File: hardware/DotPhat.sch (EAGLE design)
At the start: 61 parts, among them CN1 1X4-BIG, IC1 CAT24M010TS, IC3 SI1145, J2 RASPBERRYPI-40-PIN-GPIO_PTH, J3 USB-MICROB, Q1 BSH103, U1 ATMEGA328P-MU-QFN32, U2 TMP102, U3 ATSHA204-TSU, U4 W25Q32FV, X2 MC-RTC-RV-4162-C7-I2C, X3 S4B-ZR

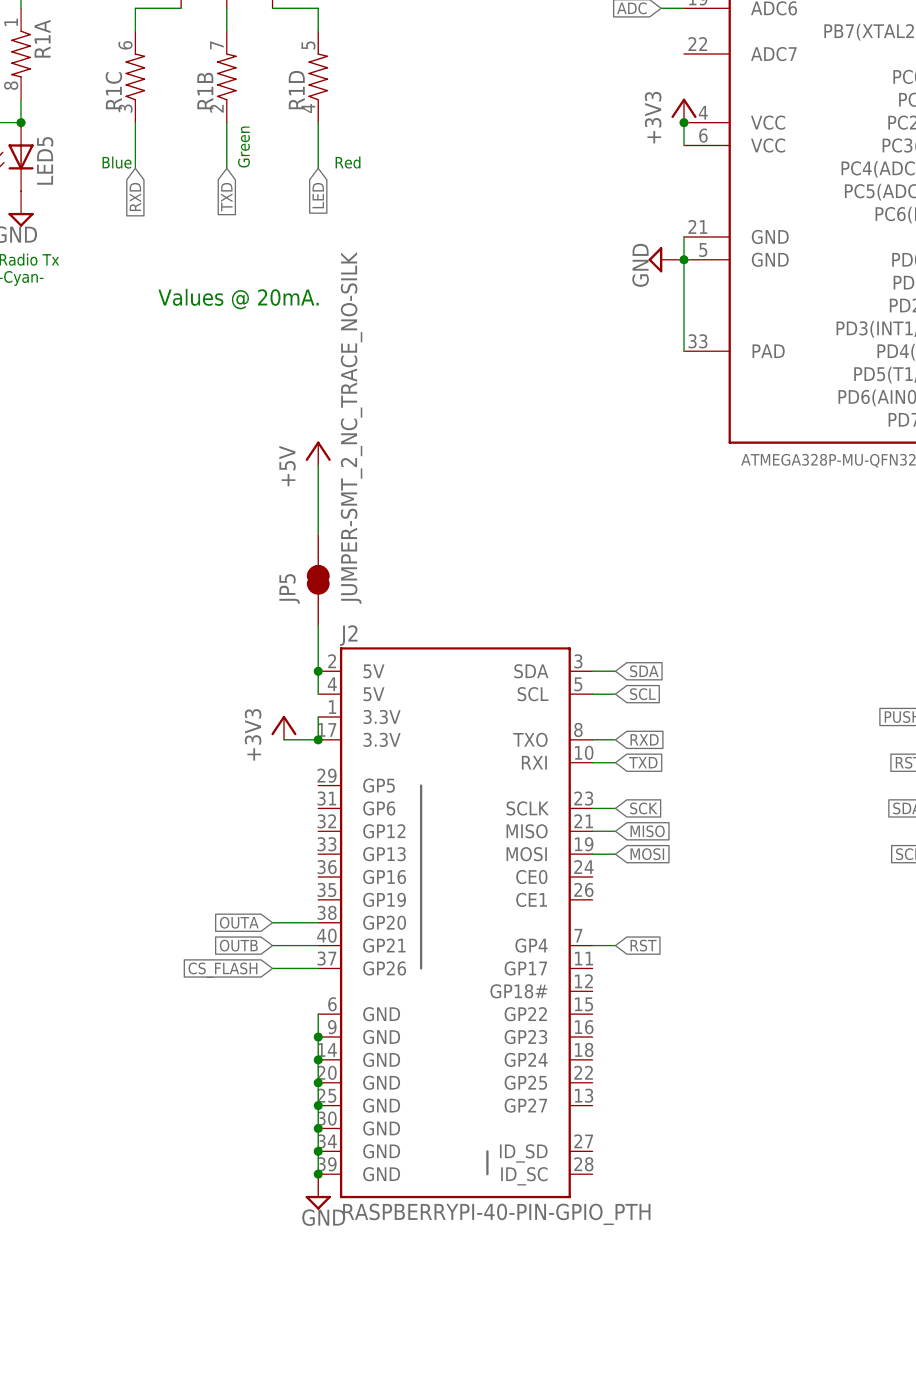
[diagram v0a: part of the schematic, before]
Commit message: Beta: initial arrange of solar
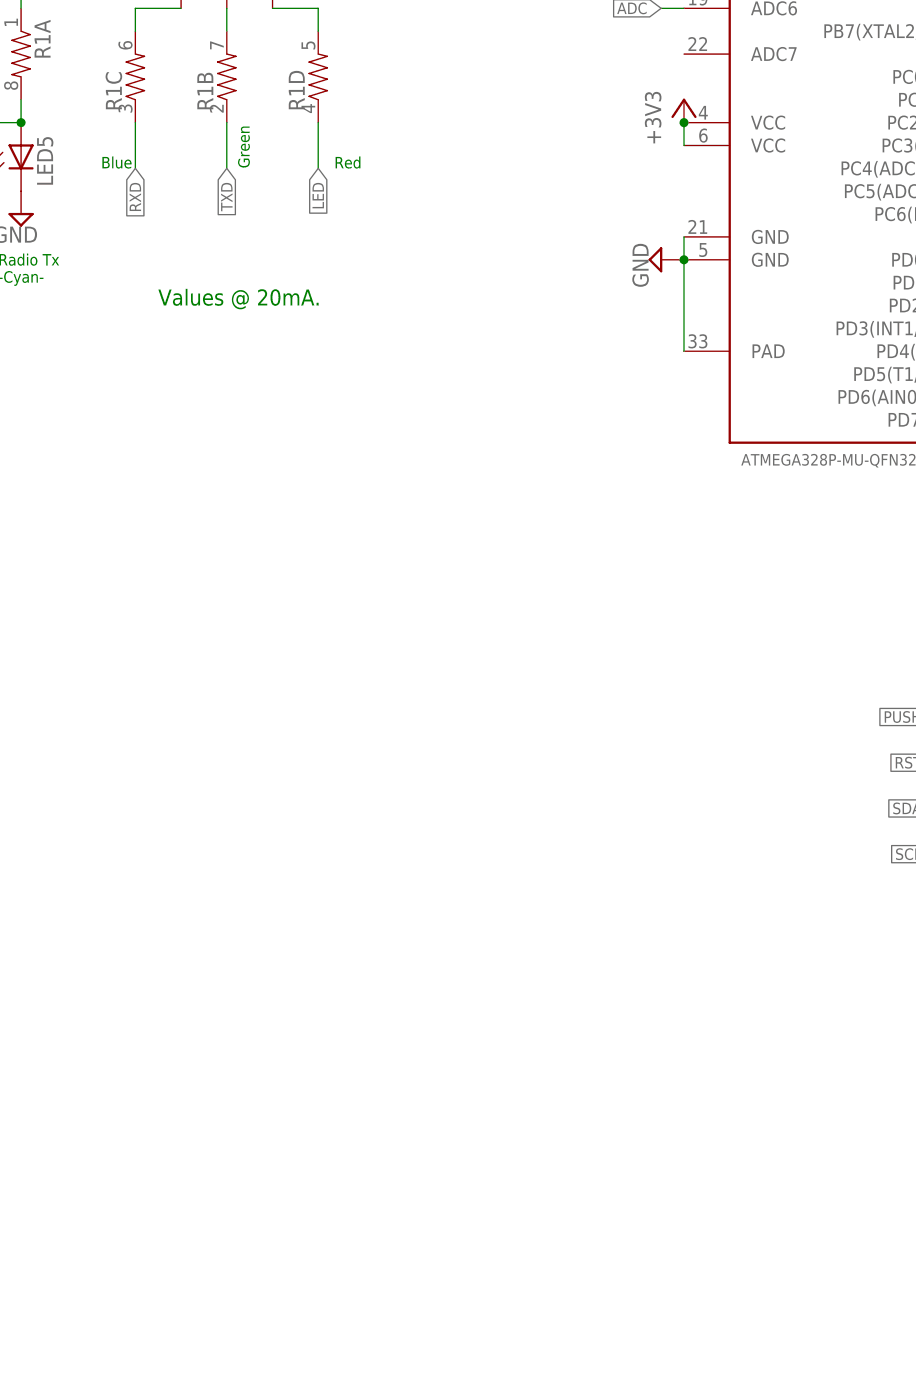
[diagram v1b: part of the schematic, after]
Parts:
- removed J2: RASPBERRYPI-40-PIN-GPIO_PTH, SparkFun-Connectors:RASPBERRYPI-40-PIN-GPIO_PTH
- removed JP5: JUMPER-SMT_2_NC_TRACE_NO-SILK, SparkFun-Jumpers:JUMPER-SMT_2_NC_TRACE_NO-SILK
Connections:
- removed net N$36: J2.5V@2, J2.5V@4, JP5.1
- net +3V3: no longer J2.3.3V@1, J2.3.3V@17
- net +5V: no longer JP5.2
- net CS_FLASH: no longer J2.GP26
- net GND: no longer J2.GND@14, J2.GND@20, J2.GND@25, J2.GND@30, J2.GND@34, J2.GND@39, J2.GND@6, J2.GND@9
- net MISO: no longer J2.MISO
- net MOSI: no longer J2.MOSI
- net OUTA: no longer J2.GP20
- net OUTB: no longer J2.GP21
- net RST: no longer J2.GP4
- net RXD: no longer J2.TXO
- net SCK: no longer J2.SCLK
- net SCL: no longer J2.SCL
- net SDA: no longer J2.SDA
- net TXD: no longer J2.RXI
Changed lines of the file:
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@@
 <part name="+3V14" library="supply1" deviceset="+3V3" device=""/>
 <part name="LED1" library="led" deviceset="GM1WA55311A" device=""/>
-<part name="J2" library="SparkFun-Connectors" deviceset="RASPBERRYPI-40-PIN-GPIO" device="_PTH"/>
 <part name="LOGO1" library="Spark" deviceset="OSHW-LOGO" device="S"/>
 <part name="SUPPLY29" library="supply2" deviceset="GND" device=""/>
@@
 <part name="R7" library="SparkFun" deviceset="RESISTOR-ARRAY" device="0603-ARV" value="4.7kΩ"/>
 <part name="+3V8" library="supply1" deviceset="+3V3" device=""/>
-<part name="+3V3" library="supply1" deviceset="+3V3" device=""/>
-<part name="SUPPLY1" library="supply2" deviceset="GND" device=""/>
 <part name="JP1" library="adafruit" deviceset="PINHD-1X6" device=""/>
 <part name="+3V6" library="supply1" deviceset="+3V3" device=""/>
@@
 <part name="SUPPLY7" library="supply2" deviceset="GND" device=""/>
 <part name="X3" library="con-jst" deviceset="?4B-ZR" device="S"/>
-<part name="P+1" library="supply1" deviceset="+5V" device=""/>
 <part name="P+2" library="supply1" deviceset="+5V" device=""/>
 <part name="LED2" library="SparkFun" deviceset="LED" device="0603"/>
@@
 <part name="SUPPLY37" library="supply2" deviceset="GND" device=""/>
 <part name="+3V23" library="supply1" deviceset="+3V3" device=""/>
-<part name="JP5" library="SparkFun-Jumpers" deviceset="JUMPER-SMT_2_NC_TRACE" device="_NO-SILK"/>
 </parts>
 <sheets>
@@
 <instance part="+3V14" gate="G$1" x="-22.86" y="81.28"/>
 <instance part="LED1" gate="G$1" x="-22.86" y="73.66"/>
-<instance part="J2" gate="G$1" x="2.54" y="-30.48"/>
 <instance part="LOGO1" gate="G$1" x="-22.86" y="104.14"/>
 <instance part="SUPPLY29" gate="GND" x="160.02" y="142.24" rot="R90"/>
@@
 <instance part="R7" gate="D" x="78.74" y="-25.4"/>
 <instance part="+3V8" gate="G$1" x="101.6" y="-2.54"/>
-<instance part="+3V3" gate="G$1" x="-16.51" y="-10.16"/>
-<instance part="SUPPLY1" gate="GND" x="-12.7" y="-63.5"/>
 <instance part="JP1" gate="A" x="63.5" y="118.11"/>
 <instance part="+3V6" gate="G$1" x="43.18" y="115.57" rot="R90"/>
@@
 <instance part="X3" gate="-3" x="111.76" y="120.65"/>
 <instance part="X3" gate="-4" x="111.76" y="118.11"/>
-<instance part="P+1" gate="1" x="-12.7" y="20.32"/>
 <instance part="P+2" gate="1" x="83.82" y="118.11" rot="R90"/>
 <instance part="LED2" gate="G$1" x="129.54" y="142.24" rot="R90"/>
@@
 <instance part="SUPPLY37" gate="GND" x="170.18" y="-228.6" rot="MR0"/>
 <instance part="+3V23" gate="G$1" x="149.86" y="-203.2"/>
-<instance part="JP5" gate="G$1" x="-12.7" y="5.08" rot="R90"/>
 </instances>
 <busses>
@@
 <pinref part="Y1" gate="G$1" pin="2"/>
 <pinref part="SUPPLY30" gate="GND" pin="GND"/>
-</segment>
-<segment>
-<pinref part="J2" gate="G$1" pin="GND@6"/>
-<pinref part="J2" gate="G$1" pin="GND@9"/>
-<wire x1="-12.7" y1="-43.18" x2="-12.7" y2="-45.72" width="0.1524" layer="91"/>
-<pinref part="J2" gate="G$1" pin="GND@14"/>
-<wire x1="-12.7" y1="-45.72" x2="-12.7" y2="-48.26" width="0.1524" layer="91"/>
-<junction x="-12.7" y="-45.72"/>
-<pinref part="J2" gate="G$1" pin="GND@20"/>
-<wire x1="-12.7" y1="-48.26" x2="-12.7" y2="-50.8" width="0.1524" layer="91"/>
-<junction x="-12.7" y="-48.26"/>
-<pinref part="J2" gate="G$1" pin="GND@25"/>
-<wire x1="-12.7" y1="-50.8" x2="-12.7" y2="-53.34" width="0.1524" layer="91"/>
-<junction x="-12.7" y="-50.8"/>
-<pinref part="J2" gate="G$1" pin="GND@30"/>
-<wire x1="-12.7" y1="-53.34" x2="-12.7" y2="-55.88" width="0.1524" layer="91"/>
-<junction x="-12.7" y="-53.34"/>
-<pinref part="J2" gate="G$1" pin="GND@34"/>
-<wire x1="-12.7" y1="-55.88" x2="-12.7" y2="-58.42" width="0.1524" layer="91"/>
-<junction x="-12.7" y="-55.88"/>
-<pinref part="J2" gate="G$1" pin="GND@39"/>
-<wire x1="-12.7" y1="-58.42" x2="-12.7" y2="-60.96" width="0.1524" layer="91"/>
-<junction x="-12.7" y="-58.42"/>
-<pinref part="SUPPLY1" gate="GND" pin="GND"/>
-<junction x="-12.7" y="-60.96"/>
 </segment>
 <segment>
@@
 </segment>
 <segment>
-<pinref part="J2" gate="G$1" pin="SDA"/>
-<wire x1="17.78" y1="-5.08" x2="20.32" y2="-5.08" width="0.1524" layer="91"/>
-<label x="20.32" y="-5.08" size="1.27" layer="95" xref="yes"/>
-</segment>
-<segment>
 <pinref part="CN1" gate="G$1" pin="1"/>
 <wire x1="76.2" y1="-72.39" x2="68.58" y2="-72.39" width="0.1524" layer="91"/>
@@
 <wire x1="66.04" y1="-15.24" x2="55.88" y2="-15.24" width="0.1524" layer="91"/>
 <junction x="66.04" y="-15.24"/>
-</segment>
-<segment>
-<pinref part="J2" gate="G$1" pin="GP4"/>
-<wire x1="17.78" y1="-35.56" x2="20.32" y2="-35.56" width="0.1524" layer="91"/>
-<label x="20.32" y="-35.56" size="1.27" layer="95" xref="yes"/>
 </segment>
 <segment>
@@
 </segment>
 <segment>
-<pinref part="J2" gate="G$1" pin="3.3V@1"/>
-<pinref part="J2" gate="G$1" pin="3.3V@17"/>
-<wire x1="-12.7" y1="-10.16" x2="-12.7" y2="-12.7" width="0.1524" layer="91"/>
-<wire x1="-12.7" y1="-12.7" x2="-16.51" y2="-12.7" width="0.1524" layer="91"/>
-<junction x="-12.7" y="-12.7"/>
-<pinref part="+3V3" gate="G$1" pin="+3V3"/>
-</segment>
-<segment>
 <pinref part="JP1" gate="A" pin="5"/>
 <wire x1="60.96" y1="115.57" x2="45.72" y2="115.57" width="0.1524" layer="91"/>
@@
 </segment>
 <segment>
-<pinref part="J2" gate="G$1" pin="MOSI"/>
-<wire x1="17.78" y1="-25.4" x2="20.32" y2="-25.4" width="0.1524" layer="91"/>
-<label x="20.32" y="-25.4" size="1.27" layer="95" xref="yes"/>
-</segment>
-<segment>
 <pinref part="JP1" gate="A" pin="1"/>
 <wire x1="60.96" y1="125.73" x2="52.07" y2="125.73" width="0.1524" layer="91"/>
@@
 </segment>
 <segment>
-<pinref part="J2" gate="G$1" pin="MISO"/>
-<wire x1="17.78" y1="-22.86" x2="20.32" y2="-22.86" width="0.1524" layer="91"/>
-<label x="20.32" y="-22.86" size="1.27" layer="95" xref="yes"/>
-</segment>
-<segment>
 <pinref part="JP1" gate="A" pin="2"/>
 <wire x1="60.96" y1="123.19" x2="52.07" y2="123.19" width="0.1524" layer="91"/>
@@
 <pinref part="R1" gate="B" pin="1"/>
 </segment>
-<segment>
-<pinref part="J2" gate="G$1" pin="RXI"/>
-<wire x1="17.78" y1="-15.24" x2="20.32" y2="-15.24" width="0.1524" layer="91"/>
-<label x="20.32" y="-15.24" size="1.27" layer="95" xref="yes"/>
-</segment>
 </net>
 <net name="SCK" class="0">
@@
 </segment>
 <segment>
-<pinref part="J2" gate="G$1" pin="SCLK"/>
-<wire x1="17.78" y1="-20.32" x2="20.32" y2="-20.32" width="0.1524" layer="91"/>
-<label x="20.32" y="-20.32" size="1.27" layer="95" xref="yes"/>
-</segment>
-<segment>
 <pinref part="JP1" gate="A" pin="3"/>
 <wire x1="60.96" y1="120.65" x2="52.07" y2="120.65" width="0.1524" layer="91"/>
@@
 </segment>
 <segment>
-<pinref part="J2" gate="G$1" pin="SCL"/>
-<wire x1="17.78" y1="-7.62" x2="20.32" y2="-7.62" width="0.1524" layer="91"/>
-<label x="20.32" y="-7.62" size="1.27" layer="95" xref="yes"/>
-</segment>
-<segment>
 <pinref part="CN1" gate="G$1" pin="2"/>
 <wire x1="76.2" y1="-74.93" x2="68.58" y2="-74.93" width="0.1524" layer="91"/>
@@
 <label x="-33.02" y="50.8" size="1.27" layer="95" rot="R270" xref="yes"/>
 <pinref part="R1" gate="C" pin="1"/>
-</segment>
-<segment>
-<pinref part="J2" gate="G$1" pin="TXO"/>
-<wire x1="17.78" y1="-12.7" x2="20.32" y2="-12.7" width="0.1524" layer="91"/>
-<label x="20.32" y="-12.7" size="1.27" layer="95" xref="yes"/>
 </segment>
 </net>
@@
 <wire x1="76.2" y1="22.86" x2="78.74" y2="22.86" width="0.1524" layer="91"/>
 <label x="78.74" y="22.86" size="1.27" layer="95" xref="yes"/>
-</segment>
-<segment>
-<pinref part="J2" gate="G$1" pin="GP21"/>
-<wire x1="-12.7" y1="-35.56" x2="-17.78" y2="-35.56" width="0.1524" layer="91"/>
-<label x="-17.78" y="-35.56" size="1.27" layer="95" rot="R180" xref="yes"/>
 </segment>
 </net>
@@
 <label x="86.36" y="120.65" size="1.27" layer="95" rot="R180" xref="yes"/>
 </segment>
-<segment>
-<pinref part="J2" gate="G$1" pin="GP20"/>
-<wire x1="-12.7" y1="-33.02" x2="-17.78" y2="-33.02" width="0.1524" layer="91"/>
-<label x="-17.78" y="-33.02" size="1.27" layer="95" rot="R180" xref="yes"/>
-</segment>
 </net>
 <net name="N$6" class="0">
@@
 <pinref part="C9" gate="G$1" pin="1"/>
 <junction x="134.62" y="-35.56"/>
-</segment>
-<segment>
-<pinref part="JP5" gate="G$1" pin="2"/>
-<pinref part="P+1" gate="1" pin="+5V"/>
-<wire x1="-12.7" y1="10.16" x2="-12.7" y2="17.78" width="0.1524" layer="91"/>
 </segment>
 </net>
@@
 <pinref part="U2" gate="G$1" pin="ALERT"/>
 <wire x1="238.76" y1="5.08" x2="243.84" y2="5.08" width="0.1524" layer="91"/>
-</segment>
-<segment>
-<pinref part="J2" gate="G$1" pin="GP26"/>
-<wire x1="-12.7" y1="-38.1" x2="-17.78" y2="-38.1" width="0.1524" layer="91"/>
-<label x="-17.78" y="-38.1" size="1.27" layer="95" rot="R180" xref="yes"/>
 </segment>
 </net>
@@
 </segment>
 </net>
-<net name="N$36" class="0">
-<segment>
-<pinref part="J2" gate="G$1" pin="5V@4"/>
-<pinref part="J2" gate="G$1" pin="5V@2"/>
-<wire x1="-12.7" y1="-7.62" x2="-12.7" y2="-5.08" width="0.1524" layer="91"/>
-<pinref part="JP5" gate="G$1" pin="1"/>
-<wire x1="-12.7" y1="-5.08" x2="-12.7" y2="0" width="0.1524" layer="91"/>
-<junction x="-12.7" y="-5.08"/>
-</segment>
-</net>
